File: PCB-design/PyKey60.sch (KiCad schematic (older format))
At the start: 227 parts, among them J1 USB_C_Receptacle_USB2.0, J2 Conn_01x03, J3 Conn_01x04, J4 Conn_01x06, SW1 SW_SPST, SW2 SW_SPDT, U1 CherryMX_LTST-A683CEGBW, U10 CherryMX_LTST-A683CEGBW, U11 CherryMX_LTST-A683CEGBW, U12 CherryMX_LTST-A683CEGBW, U13 CherryMX_LTST-A683CEGBW, U14 CherryMX_LTST-A683CEGBW, U15 CherryMX_LTST-A683CEGBW, U16 CherryMX_LTST-A683CEGBW, U17 CherryMX_LTST-A683CEGBW, U18 CherryMX_LTST-A683CEGBW, U19 CherryMX_LTST-A683CEGBW, U2 CherryMX_LTST-A683CEGBW, U20 CherryMX_LTST-A683CEGBW, U21 CherryMX_LTST-A683CEGBW, U22 CherryMX_LTST-A683CEGBW, U23 CherryMX_LTST-A683CEGBW, U24 CherryMX_LTST-A683CEGBW, U25 CherryMX_LTST-A683CEGBW, U26 CherryMX_LTST-A683CEGBW, U27 CherryMX_LTST-A683CEGBW, U28 CherryMX_LTST-A683CEGBW, U29 CherryMX_LTST-A683CEGBW, U3 CherryMX_LTST-A683CEGBW, U30 CherryMX_LTST-A683CEGBW, U31 CherryMX_LTST-A683CEGBW, U32 CherryMX_LTST-A683CEGBW, U33 CherryMX_LTST-A683CEGBW, U34 CherryMX_LTST-A683CEGBW, U35 CherryMX_LTST-A683CEGBW, U36 CherryMX_LTST-A683CEGBW, U37 CherryMX_LTST-A683CEGBW, U38 CherryMX_LTST-A683CEGBW, U39 CherryMX_LTST-A683CEGBW, U4 CherryMX_LTST-A683CEGBW, U40 CherryMX_LTST-A683CEGBW, U41 CherryMX_LTST-A683CEGBW, U42 CherryMX_LTST-A683CEGBW, U43 CherryMX_LTST-A683CEGBW, U44 CherryMX_LTST-A683CEGBW, U45 CherryMX_LTST-A683CEGBW, U46 CherryMX_LTST-A683CEGBW, U47 CherryMX_LTST-A683CEGBW, U48 CherryMX_LTST-A683CEGBW, U49 CherryMX_LTST-A683CEGBW, U5 CherryMX_LTST-A683CEGBW, U50 CherryMX_LTST-A683CEGBW, U51 CherryMX_LTST-A683CEGBW, U52 CherryMX_LTST-A683CEGBW, U53 CherryMX_LTST-A683CEGBW, U54 CherryMX_LTST-A683CEGBW, U55 CherryMX_LTST-A683CEGBW, U56 CherryMX_LTST-A683CEGBW, U57 CherryMX_LTST-A683CEGBW, U58 CherryMX_LTST-A683CEGBW, U59 CherryMX_LTST-A683CEGBW, U6 CherryMX_LTST-A683CEGBW, U60 CherryMX_LTST-A683CEGBW, U61 CherryMX_LTST-A683CEGBW, U62 RP2040, U63 USBLC6-2SC6, U64 W25Q128JVS, U65 AMS1117-3.3, U7 CherryMX_LTST-A683CEGBW, U8 CherryMX_LTST-A683CEGBW, U9 CherryMX_LTST-A683CEGBW, Y1 12MHz

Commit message: PyKey87
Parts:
- removed D62: RED, LED_SMD:LED_0603_1608Metric, symbol Device:LED
- removed LS1: Speaker, Buzzer_Beeper:Buzzer_Mallory_AST1109MLTRQ, symbol Device:Speaker
- removed R8: 1k, Resistor_SMD:R_0603_1608Metric, symbol Device:R
- added D62, D63, D64, D65, D66, D67, D68, D69, D70, D71, D72, D73, D74, D75, D76, D77, D78, D79, D80, D81, D82, D83, D84, D85, D86, D87, D88: D, Diode_SMD:D_SOD-123, symbol Device:D
- added U66, U67, U68, U69, U70, U71, U72, U73, U74, U75, U76, U77, U78, U80, U81, U82, U83, U84, U85, U86, U88: CherryMX_LTST-A683CEGBW, CherryMX_PCB_KailhSocket_LTST-A683CEGBW-Rotated-HS:CherryMX_1.00u_PCB_KailhSocket_LTST-A683CEGBW-Rotated-HS, symbol CherryMX:CherryMX_LTST-A683CEGBW
- added U79, U87, U89, U90, U91, U92: CherryMX_LTST-A683CEGBW, CherryMX_PCB_KailhSocket_StabWireTop_LTST-A683CEGBW-Rotated-HS:CherryMX_2.00u_PCB_KailhSocket_StabWireTop_LTST-A683CEGB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, symbol CherryMX:CherryMX_LTST-A683CEGBW
- J1: symbol Connector:USB_C_Receptacle_USB2.0 -> PyKey60-rescue:USB_C_Receptacle_USB2.0-Connector
- U63: symbol Power_Protection:USBLC6-2SC6 -> PyKey60-rescue:USBLC6-2SC6-Power_Protection
- U64: symbol Memory_Flash:W25Q128JVS -> PyKey60-rescue:W25Q128JVS-Memory_Flash
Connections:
- net labels added: COL15, COL16, COL17, RGBData0, ROW0
- net labels removed: LED, SPEAKER
- wire segments 1039 -> 1307
- no-connect marks 7 -> 5

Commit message: adding more connections
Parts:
- removed D63: D, Diode_SMD:D_SOD-123, symbol Device:D
- removed U67: CherryMX_LTST-A683CEGBW, CherryMX_PCB_KailhSocket_LTST-A683CEGBW-Rotated-HS:CherryMX_1.00u_PCB_KailhSocket_LTST-A683CEGBW-Rotated-HS, symbol CherryMX:CherryMX_LTST-A683CEGBW
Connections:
- wire segments 1307 -> 1295
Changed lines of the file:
@@
 	4200 1650 4300 1650
 Wire Wire Line
-	3800 1100 3750 1100
-Wire Wire Line
 	3750 4550 3600 4550
 Wire Wire Line
@@
 	2500 1650 2500 2300
 Wire Wire Line
-	2500 1100 2600 1100
-Wire Wire Line
 	2400 1650 2500 1650
 Wire Wire Line
@@
 	7700 1100 7600 1100
 $Comp
-L CherryMX:CherryMX_LTST-A683CEGBW U67
-U 1 1 622342B5
-P 3350 1000
-F 0 "U67" H 3350 1385 50  0000 C CNN
-F 1 "CherryMX_LTST-A683CEGBW" H 3350 1294 50  0000 C CNN
-F 2 "CherryMX_PCB_KailhSocket_LTST-A683CEGBW-Rotated-HS:CherryMX_1.00u_PCB_KailhSocket_LTST-A683CEGBW-Rotated-HS" H 3350 900 50  0001 C CNN
-F 3 "" H 3350 900 50  0001 C CNN
-	1    3350 1000
-	1    0    0    -1
-$EndComp
-$Comp
-L Device:D D63
-U 1 1 622342BB
-P 2800 900
-F 0 "D63" H 2800 1117 50  0000 C CNN
-F 1 "D" H 2800 1026 50  0000 C CNN
-F 2 "Diode_SMD:D_SOD-123" H 2800 900 50  0001 C CNN
-F 3 "~" H 2800 900 50  0001 C CNN
-	1    2800 900
-	1    0    0    -1
-$EndComp
-$Comp
 L CherryMX:CherryMX_LTST-A683CEGBW U68
 U 1 1 622342C1
@@
 COL2
 Wire Wire Line
-	2650 1200 2650 900
-Wire Wire Line
-	2650 1200 3900 1200
-Wire Wire Line
 	3900 1200 3900 900
 Wire Wire Line
-	2950 900  3050 900
-Wire Wire Line
 	4200 900  4300 900
 Wire Wire Line
 	3800 350  3750 350
 Wire Wire Line
-	3750 350  3750 900
-Wire Wire Line
-	3650 900  3750 900
-Connection ~ 3750 900
-Wire Wire Line
 	3900 1200 5150 1200
 Wire Wire Line
 	5150 1200 5150 900
-Connection ~ 3900 1200
 Wire Wire Line
 	5150 1200 6450 1200
@@
 	16700 1150 17000 1150
 Wire Wire Line
-	2700 1000 2700 1100
-Wire Wire Line
-	2700 1100 3050 1100
-Wire Wire Line
-	3650 1000 4000 1000
-Wire Wire Line
-	4000 1000 4000 1100
-Wire Wire Line
-	4000 1100 4300 1100
-Wire Wire Line
 	4900 1000 5200 1000
 Wire Wire Line
@@
 	6500 1100 6850 1100
 $Comp
-L power:GND #PWR0239
-U 1 1 622343F7
-P 2950 1000
-F 0 "#PWR0239" H 2950 750 50  0001 C CNN
-F 1 "GND" H 2955 827 50  0000 C CNN
-F 2 "" H 2950 1000 50  0001 C CNN
-F 3 "" H 2950 1000 50  0001 C CNN
-	1    2950 1000
-	0    1    1    0
-$EndComp
-$Comp
 L power:GND #PWR0240
 U 1 1 622343FD
@@
 $EndComp
 Wire Wire Line
-	2950 1000 3050 1000
-Wire Wire Line
 	4200 1000 4300 1000
 Wire Wire Line
@@
 	14450 1050 14350 1050
 $Comp
-L power:+3V3 #PWR0252
-U 1 1 62234452
-P 3700 1100
-F 0 "#PWR0252" H 3700 950 50  0001 C CNN
-F 1 "+3V3" H 3715 1273 50  0000 C CNN
-F 2 "" H 3700 1100 50  0001 C CNN
-F 3 "" H 3700 1100 50  0001 C CNN
-	1    3700 1100
-	0    1    1    0
-$EndComp
-$Comp
 L power:+3V3 #PWR0253
 U 1 1 62234458
@@
 	4950 1100 4900 1100
 Wire Wire Line
-	3700 1100 3650 1100
-Wire Wire Line
 	7450 1100 7500 1100
 Wire Wire Line
@@
 	0    1    1    0
 $EndComp
-Connection ~ 2650 1200
 Wire Wire Line
 	2450 1100 2400 1100
@@
 $EndComp
 Wire Wire Line
-	2400 1000 2700 1000
-Wire Wire Line
 	1700 1100 1800 1100
 Text GLabel 1700 1100 0    60   Input ~ 0
 RGBData0
 Connection ~ 1250 1200
-Wire Wire Line
-	1250 1200 2650 1200
 Connection ~ 2500 900
 Wire Wire Line
@@
 	7700 350  7600 350
 Wire Wire Line
-	3750 900  3750 1650
-Wire Wire Line
 	5050 900  5050 1650
 Wire Wire Line
@@
 Wire Wire Line
 	11200 9650 11350 9650
+Wire Wire Line
+	3750 350  3750 1650
+Wire Wire Line
+	3850 1000 3850 1100
+Wire Wire Line
+	2400 1000 3850 1000
+Wire Wire Line
+	3850 1100 4300 1100
+Connection ~ 3900 1200
+Wire Wire Line
+	1250 1200 3900 1200
 $EndSCHEMATC

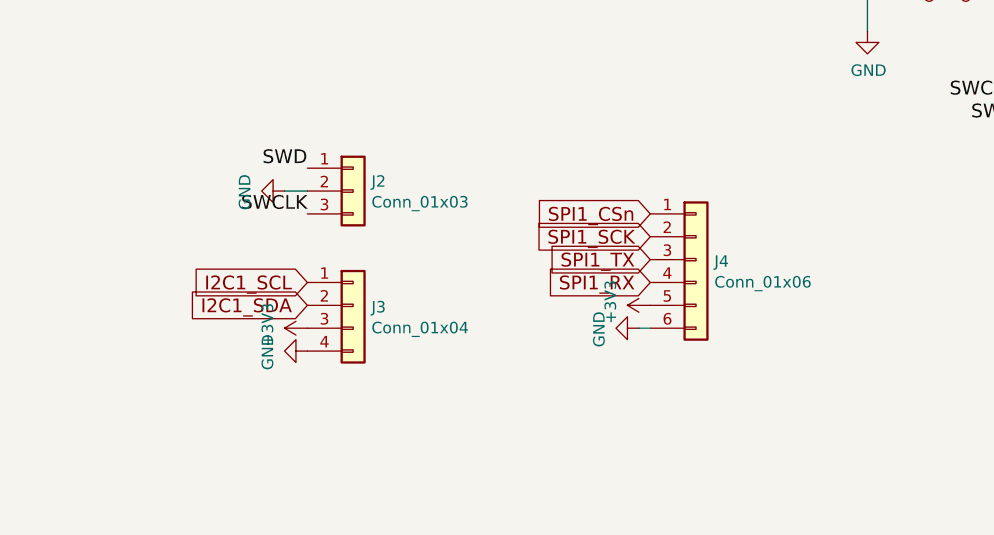
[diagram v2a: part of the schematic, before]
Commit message: Remove I2C and SPI due to space
Not enough space to route additional columns; debugging should be ok via SWD.
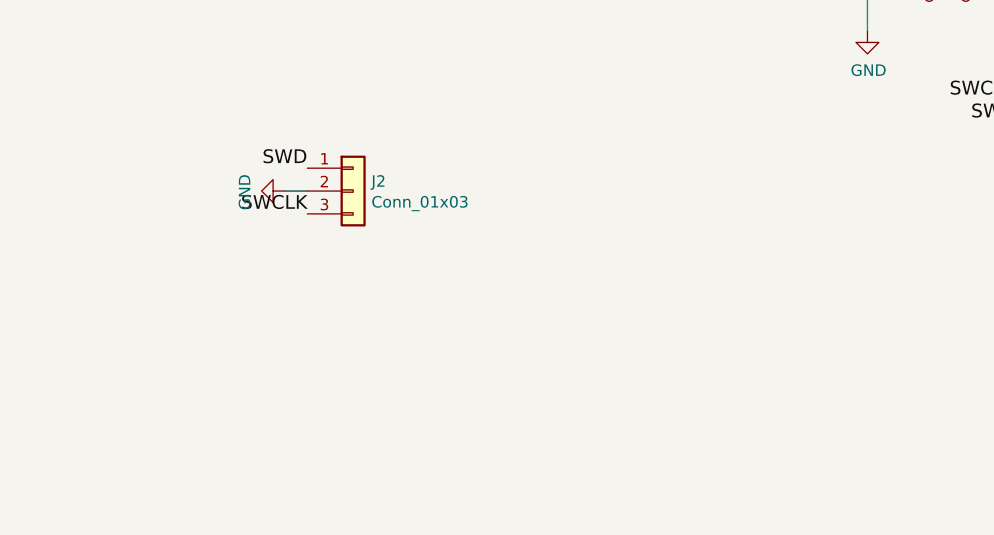
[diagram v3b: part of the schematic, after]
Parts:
- removed J3: Conn_01x04, Connector_PinHeader_2.54mm:PinHeader_1x04_P2.54mm_Vertical, symbol Connector_Generic:Conn_01x04
- removed J4: Conn_01x06, Connector_PinHeader_2.54mm:PinHeader_1x06_P2.54mm_Vertical, symbol Connector_Generic:Conn_01x06
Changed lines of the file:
@@
 	11200 10350 11350 10350
-$Comp
-L Connector_Generic:Conn_01x04 J3
-U 1 1 66F2047C
-P 5800 10900
-F 0 "J3" H 5880 10892 50  0000 L CNN
-F 1 "Conn_01x04" H 5880 10801 50  0000 L CNN
-F 2 "Connector_PinHeader_2.54mm:PinHeader_1x04_P2.54mm_Vertical" H 5800 10900 50  0001 C CNN
-F 3 "~" H 5800 10900 50  0001 C CNN
-	1    5800 10900
-	1    0    0    -1
-$EndComp
-$Comp
-L power:GND #PWR07
-U 1 1 66F2381A
-P 5600 11100
-F 0 "#PWR07" H 5600 10850 50  0001 C CNN
-F 1 "GND" H 5605 10927 50  0000 C CNN
-F 2 "" H 5600 11100 50  0001 C CNN
-F 3 "" H 5600 11100 50  0001 C CNN
-	1    5600 11100
-	0    1    1    0
-$EndComp
-$Comp
-L power:+3V3 #PWR06
-U 1 1 66F23A9B
-P 5600 11000
-F 0 "#PWR06" H 5600 10850 50  0001 C CNN
-F 1 "+3V3" H 5615 11173 50  0000 C CNN
-F 2 "" H 5600 11000 50  0001 C CNN
-F 3 "" H 5600 11000 50  0001 C CNN
-	1    5600 11000
-	0    -1   -1   0
-$EndComp
-Text GLabel 5600 10900 0    60   Input ~ 0
-I2C1_SDA
-Text GLabel 5600 10800 0    60   Input ~ 0
-I2C1_SCL
-$Comp
-L Connector_Generic:Conn_01x06 J4
-U 1 1 671A6692
-P 7300 10700
-F 0 "J4" H 7380 10692 50  0000 L CNN
-F 1 "Conn_01x06" H 7380 10601 50  0000 L CNN
-F 2 "Connector_PinHeader_2.54mm:PinHeader_1x06_P2.54mm_Vertical" H 7300 10700 50  0001 C CNN
-F 3 "~" H 7300 10700 50  0001 C CNN
-	1    7300 10700
-	1    0    0    -1
-$EndComp
-Text GLabel 7100 10500 0    60   Input ~ 0
-SPI1_CSn
-Text GLabel 7100 10600 0    60   Input ~ 0
-SPI1_SCK
-Text GLabel 7100 10700 0    60   Input ~ 0
-SPI1_TX
-Text GLabel 7100 10800 0    60   Input ~ 0
-SPI1_RX
-$Comp
-L power:+3V3 #PWR08
-U 1 1 671A8F9F
-P 7100 10900
-F 0 "#PWR08" H 7100 10750 50  0001 C CNN
-F 1 "+3V3" H 7115 11073 50  0000 C CNN
-F 2 "" H 7100 10900 50  0001 C CNN
-F 3 "" H 7100 10900 50  0001 C CNN
-	1    7100 10900
-	0    -1   -1   0
-$EndComp
 $Comp
 L power:+3V3 #PWR0237
@@
 Connection ~ 15400 11500
 Wire Wire Line
-	7100 11000 7050 11000
-Wire Wire Line
 	2000 5900 2650 5900
 Connection ~ 2650 5900
@@
 	2650 5900 3150 5900
 $Comp
-L power:GND #PWR0238
-U 1 1 6153BB9E
-P 7050 11000
-F 0 "#PWR0238" H 7050 10750 50  0001 C CNN
-F 1 "GND" H 7055 10827 50  0000 C CNN
-F 2 "" H 7050 11000 50  0001 C CNN
-F 3 "" H 7050 11000 50  0001 C CNN
-	1    7050 11000
-	0    1    1    0
-$EndComp
-$Comp
 L power:PWR_FLAG #FLG0102

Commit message: Update Schematic to Reflect PCB
Also reroute +3.3V through 100nF capacitor before LED per https://optoelectronics.liteon.com/upload/download/DS35-2019-0032/LTST-A683CEGBW.PDF
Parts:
- renumbered U62 to U100, U63 to U101, U64 to U102, U65 to U103, U66 to U62, U68 to U63, U69 to U64, U70 to U65, U71 to U66, U72 to U67, U73 to U68, U74 to U69, U75 to U70, U76 to U71, U77 to U72, U78 to U73, U79 to U74, U80 to U75, U84 to U76, U89 to U77, U81 to U78, U85 to U79, U90 to U80, U82 to U81, U86 to U82, U91 to U83, U87 to U84, U83 to U85, U88 to U86, U92 to U87
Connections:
- net I2C1_SCL is gone; now on net ROW0: U100.36 (GPIO24)
- net COL15: now also U100.30 (GPIO19); no longer U100.17 (GPIO14)
- net COL16: now also U100.31 (GPIO20); no longer U100.18 (GPIO15)
- net COL17: now also U100.32 (GPIO21); no longer U100.27 (GPIO16)
- net ROW0: no longer U100.28 (GPIO17)
- net ROW1: now also U100.17 (GPIO14); no longer U100.29 (GPIO18)
- net ROW2: now also U100.18 (GPIO15); no longer U100.30 (GPIO19)
- net ROW3: now also U100.27 (GPIO16); no longer U100.31 (GPIO20)
- net ROW4: now also U100.28 (GPIO17); no longer U100.32 (GPIO21)
- net ROW5: now also U100.29 (GPIO18); no longer U100.34 (GPIO22)
- net at U28.5 (DOUT): now also U81.4 (DIN)
- net I2C1_SDA: no longer names the net of U100.35 (GPIO23)
- net SPI1_CSn: no longer names the net of U100.37 (GPIO25)
- net SPI1_RX: no longer names the net of U100.40 (GPIO28_ADC2)
- net SPI1_SCK: no longer names the net of U100.38 (GPIO26_ADC0)
- net SPI1_TX: no longer names the net of U100.39 (GPIO27_ADC1)
- no-connect marks 5 -> 11

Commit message: Reinstall LED and Speaker
I decided I like knowing when caps lock  is on and want to play Star Trek sounds on my keyboard.
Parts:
- added C100, C101, C102, C103, C78, C79, C80, C81, C82, C83, C84, C85, C86, C87, C88, C89, C90, C91, C92, C93, C94, C95, C96, C97, C98, C99: 100n, Capacitor_SMD:C_0603_1608Metric, symbol Device:C
- added D101: RED, LED_SMD:LED_0603_1608Metric, symbol Device:LED
- added LS1: Speaker, Buzzer:AST1109MLTRQ, symbol Device:Speaker
- added R8: 1k, Resistor_SMD:R_0603_1608Metric, symbol Device:R
- renumbered D64 to D63, D65 to D64, D66 to D65, D67 to D66, D68 to D67, D69 to D68, D70 to D69, D71 to D70, D72 to D71, D73 to D72, D74 to D73, D75 to D74, D76 to D75, D80 to D76, D85 to D77, D77 to D78, D81 to D79, D86 to D80, D78 to D81, D87 to D83, D83 to D84, D79 to D85, D84 to D86, D88 to D87
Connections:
- net ROW0 is gone; now on net COL5: D62.1 (K), D63.1 (K), D64.1 (K), D65.1 (K), D66.1 (K), D67.1 (K), D68.1 (K), D69.1 (K), D70.1 (K), D71.1 (K), D72.1 (K), D73.1 (K), D74.1 (K), U100.36 (GPIO24)
- net +3V3: now also C68.2, C69.2, C70.2, C71.2, C72.2, C73.2, C74.2, C75.2, C76.2, C77.2, C100.1, C100.2, C101.1, C102.1, C103.1, C78.1, C79.1, C80.1, C81.1, C82.1, C82.2, C83.1, C84.1, C85.1, C86.1, C87.1, C88.1, C88.2, C89.1, C90.1, C91.1, C92.1, C93.1, C94.1, C94.2, C95.1, C96.1, C97.1, C98.1, C99.1
- net COL10: no longer U70.2
- net COL2: now also U63.2
- net COL3: now also U64.2; no longer U63.2
- net COL4: now also U65.2; no longer U64.2
- net COL5: now also U66.2; no longer U65.2
- net COL6: now also U66.5 (DOUT), U67.2, U67.4 (DIN); no longer U66.2
- net COL7: now also U68.2; no longer U67.2
- net COL8: now also U68.5 (DOUT), U69.2, U69.4 (DIN); no longer U68.2
- net COL9: now also U70.2; no longer U69.2
- net GND: now also D101.1 (K), LS1.2; no longer C17.2, C18.2, C19.2, C20.2, C21.2, C22.2, C23.2, C24.2, C25.2, C26.2, C27.2, C28.2, C29.2, C30.2, C31.2, C32.2, C33.2, C34.2, C35.2, C36.2, C37.2, C38.2, C39.2, C40.2, C41.2, C42.2, C43.2, C44.2, C45.2, C46.2, C47.2, C48.2, C49.2, C50.2, C51.2, C52.2, C53.2, C54.2, C55.2, C56.2, C57.2, C58.2, C59.2, C60.2, C61.2, C62.2, C63.2, C64.2, C65.2, C66.2, C67.2, C68.2, C69.2, C70.2, C71.2, C72.2, C73.2, C74.2, C75.2, C76.2, C77.2
- net Speaker: now reaches U100.34 (GPIO22)
- net Speaker: now also LS1.1
- net LED: now reaches U100.39 (GPIO27_ADC1)
- net LED: now also R8.1
- new net: D101.2 (A), R8.2
- new net: C101.2, C17.2, C18.2, C19.2, C20.2, C21.2, C22.2, C23.2, C24.2, C25.2, C26.2, C67.2, C83.2, C89.2, C95.2
- new net: C102.2, C27.2, C28.2, C29.2, C30.2, C31.2, C32.2, C33.2, C34.2, C35.2, C36.2, C78.2, C84.2, C90.2, C96.2
- new net: C103.2, C37.2, C38.2, C39.2, C40.2, C41.2, C42.2, C43.2, C44.2, C45.2, C46.2, C79.2, C85.2, C91.2, C97.2
- new net: C47.2, C48.2, C49.2, C50.2, C51.2, C52.2, C53.2, C54.2, C55.2, C56.2, C80.2, C86.2, C92.2, C98.2
- new net: C57.2, C58.2, C59.2, C60.2, C61.2, C62.2, C63.2, C64.2, C65.2, C66.2, C81.2, C87.2, C93.2, C99.2
- no-connect marks 11 -> 9
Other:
- moved on the sheet: C1, C10, C11, C12, C13, C14, C15, C16, C17, C18, C19, C2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

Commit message: Reroute and round PCB
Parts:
- removed H1: MountingHole, lib.pretty:PKRHC, symbol Mechanical:MountingHole
- removed H2, H4, H6: MountingHole, lib.pretty:PKRH, symbol Mechanical:MountingHole
- removed H3, H5: MountingHole, lib.pretty:PKRHSL, symbol Mechanical:MountingHole
- removed H7: MountingHole, lib.pretty:KB_BlueMicro, symbol Mechanical:MountingHole
- added H1, H2, H3, H4, H5, H6: MountingHole_Pad, MountingHole:MountingHole_2.7mm_M2.5_Pad, symbol Mechanical:MountingHole_Pad
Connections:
- net +3V3: no longer C100.2, C68.2, C69.2, C70.2, C71.2, C72.2, C73.2, C74.2, C75.2, C76.2, C77.2, C82.2, C88.2, C94.2
- net COL11: now also U11.2, U25.2, U39.2, U52.2, U59.2
- net COL17: now also U100.37 (GPIO25); no longer U100.32 (GPIO21)
- net COL5: now also U100.39 (GPIO27_ADC1); no longer U100.36 (GPIO24)
- net GND: now also C100.2, C101.2, C102.2, C103.2, C17.2, C18.2, C19.2, C20.2, C21.2, C22.2, C23.2, C24.2, C25.2, C26.2, C27.2, C28.2, C29.2, C30.2, C31.2, C32.2, C33.2, C34.2, C35.2, C36.2, C37.2, C38.2, C39.2, C40.2, C41.2, C42.2, C43.2, C44.2, C45.2, C46.2, C47.2, C48.2, C49.2, C50.2, C51.2, C52.2, C53.2, C54.2, C55.2, C56.2, C57.2, C58.2, C59.2, C60.2, C61.2, C62.2, C63.2, C64.2, C65.2, C66.2, C67.2, C68.2, C69.2, C70.2, C71.2, C72.2, C73.2, C74.2, C75.2, C76.2, C77.2, C78.2, C79.2, C80.2, C81.2, C82.2, C83.2, C84.2, C85.2, C86.2, C87.2, C88.2, C89.2, C90.2, C91.2, C92.2, C93.2, C94.2, C95.2, C96.2, C97.2, C98.2, C99.2
- net LED: now also U100.36 (GPIO24); no longer U100.39 (GPIO27_ADC1)
- net Speaker: now also U100.32 (GPIO21); no longer U100.34 (GPIO22)

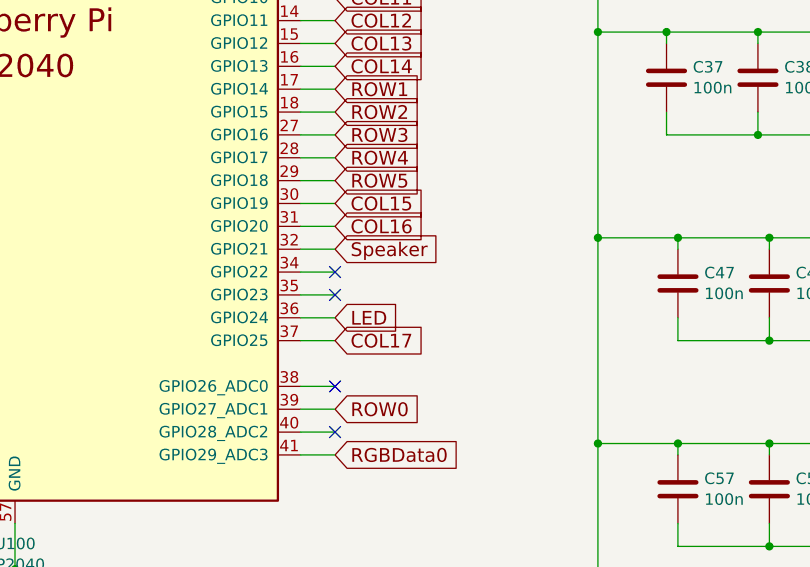
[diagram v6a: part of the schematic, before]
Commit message: Add bottom plate and I2C
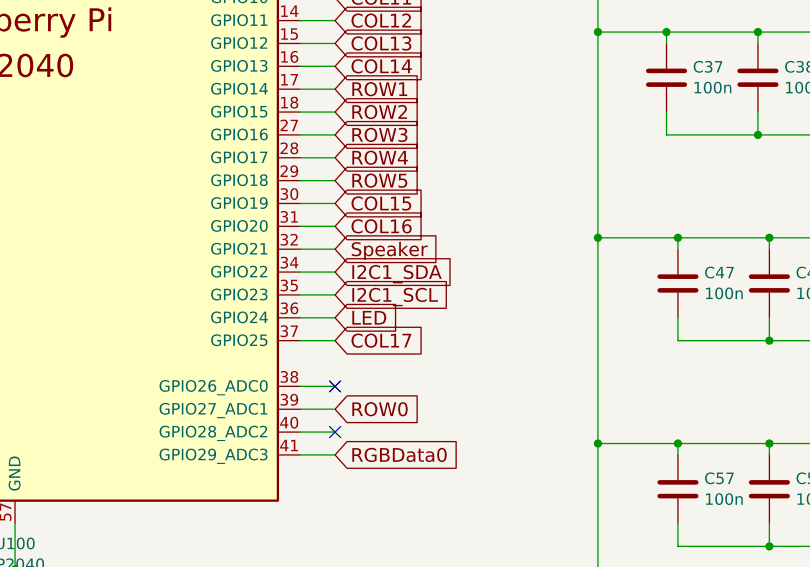
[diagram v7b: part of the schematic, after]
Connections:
- net I2C1_SDA: now reaches U100.34 (GPIO22)
- net I2C1_SCL: now reaches U100.35 (GPIO23)
- no-connect marks 9 -> 7
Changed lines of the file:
@@
 Text GLabel 11150 10500 2    60   Input ~ 0
 LED
-Text GLabel 11150 10200 2    60   Input ~ 0
-Speaker
 $Comp
 L power:GND #PWR0239
@@
 NoConn ~ 11150 11000
 NoConn ~ 11150 10800
-NoConn ~ 11150 10400
 Wire Wire Line
 	1050 1850 3700 1850
@@
 	1    0    0    -1
 $EndComp
-NoConn ~ 11150 10300
 $Comp
 L power:GND #PWR0252
@@
 Wire Wire Line
 	14950 2350 15000 2350
+Text GLabel 11150 10200 2    60   Input ~ 0
+Speaker
+Text GLabel 11150 10300 2    60   Input ~ 0
+I2C1_SDA
+Text GLabel 11150 10400 2    60   Input ~ 0
+I2C1_SCL
 $EndSCHEMATC

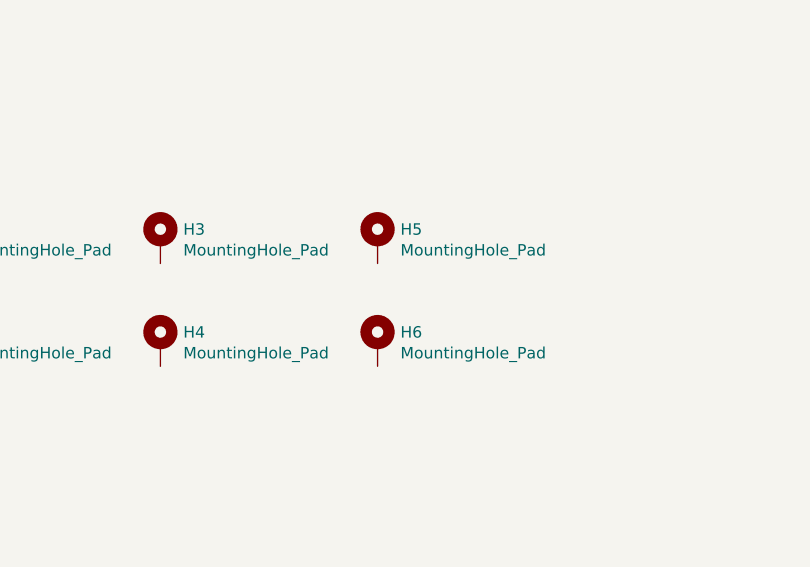
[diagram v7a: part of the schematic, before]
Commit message: Add cutout for obscured switches
Also added extra holes for feet and additional standoff
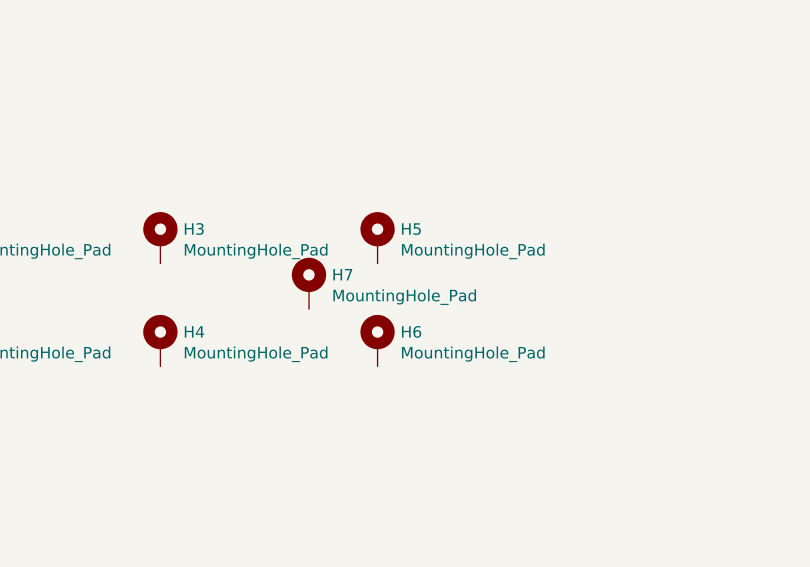
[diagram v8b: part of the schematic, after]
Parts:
- added H7: MountingHole_Pad, MountingHole:MountingHole_2.7mm_M2.5_Pad, symbol Mechanical:MountingHole_Pad
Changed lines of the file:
@@
 Text GLabel 11150 10400 2    60   Input ~ 0
 I2C1_SCL
+$Comp
+L Mechanical:MountingHole_Pad H7
+U 1 1 61B6C89D
+P 20550 7000
+F 0 "H7" H 20650 7049 50  0000 L CNN
+F 1 "MountingHole_Pad" H 20650 6958 50  0000 L CNN
+F 2 "MountingHole:MountingHole_2.7mm_M2.5_Pad" H 20550 7000 50  0001 C CNN
+F 3 "~" H 20550 7000 50  0001 C CNN
+	1    20550 7000
+	1    0    0    -1
+$EndComp
 $EndSCHEMATC
